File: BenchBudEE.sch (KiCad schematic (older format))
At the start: 0 parts

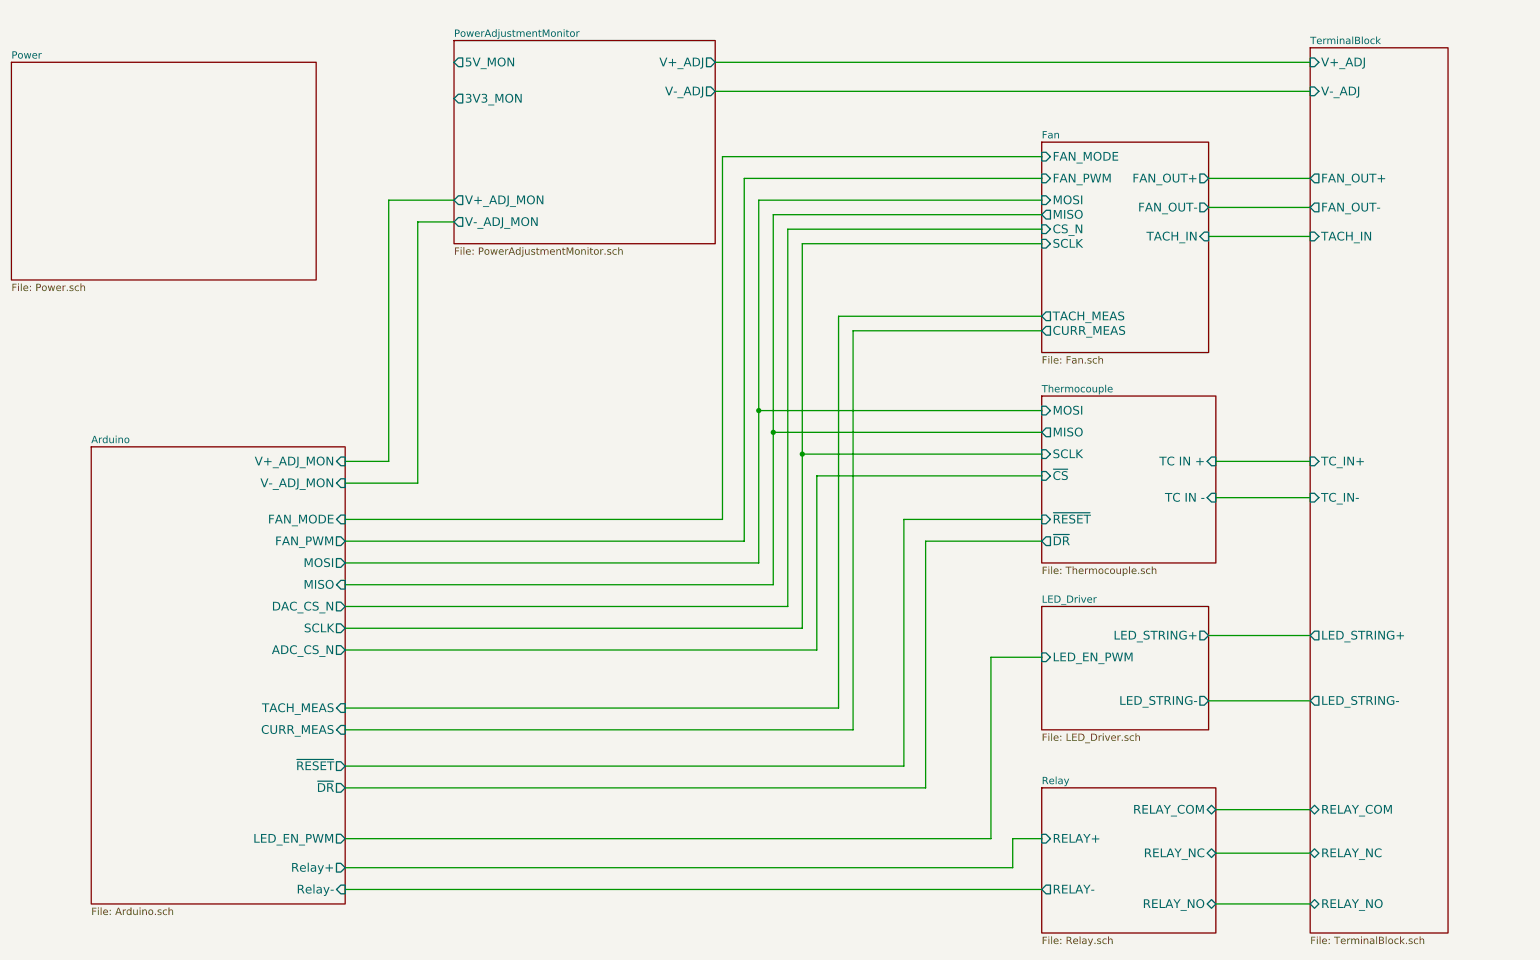
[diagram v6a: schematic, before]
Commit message: Fan driver: assc/placement
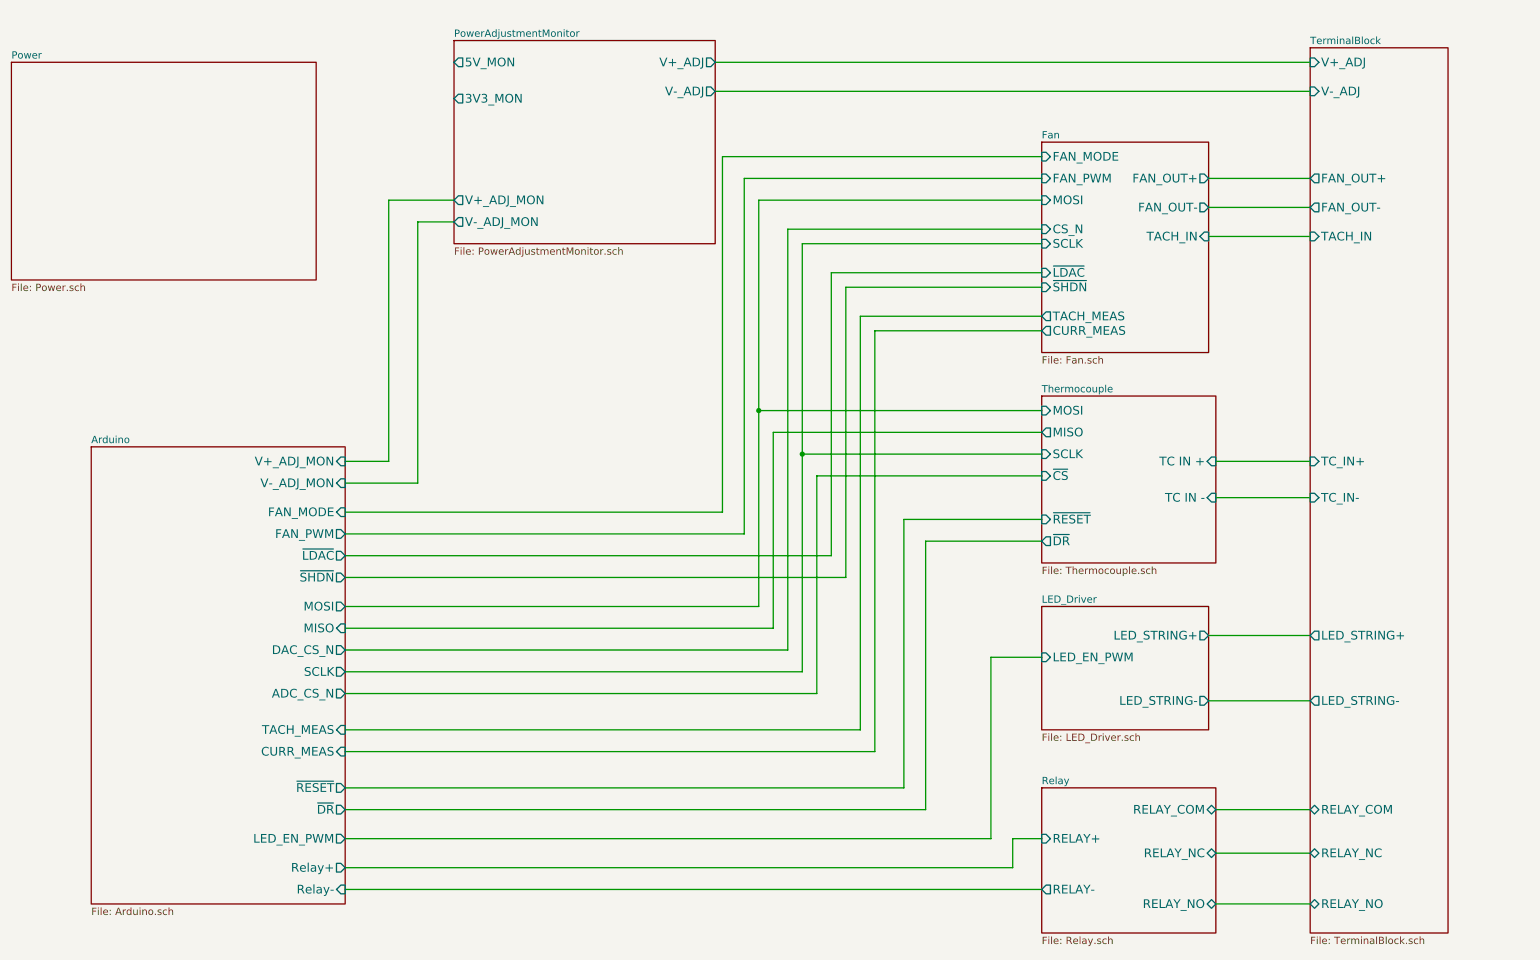
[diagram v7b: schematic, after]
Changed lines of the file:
@@
 Sheet 1 9
 Title ""
-Date "22 feb 2014"
+Date "23 feb 2014"
 Rev ""
 Comp ""
@@
 F1 "Fan.sch" 50
 F2 "MOSI" I L 8200 1950 60
-F3 "MISO" O L 8200 2050 60
-F4 "CS_N" I L 8200 2150 60
-F5 "SCLK" I L 8200 2250 60
-F6 "FAN_OUT+" O R 9350 1800 60
-F7 "TACH_IN" I R 9350 2200 60
-F8 "TACH_MEAS" O L 8200 2750 60
-F9 "CURR_MEAS" O L 8200 2850 60
-F10 "FAN_OUT-" O R 9350 2000 60
-F11 "FAN_PWM" I L 8200 1800 60
-F12 "FAN_MODE" I L 8200 1650 60
+F3 "CS_N" I L 8200 2150 60
+F4 "SCLK" I L 8200 2250 60
+F5 "FAN_OUT+" O R 9350 1800 60
+F6 "TACH_IN" I R 9350 2200 60
+F7 "TACH_MEAS" O L 8200 2750 60
+F8 "CURR_MEAS" O L 8200 2850 60
+F9 "FAN_OUT-" O R 9350 2000 60
+F10 "FAN_PWM" I L 8200 1800 60
+F11 "FAN_MODE" I L 8200 1650 60
+F12 "~LDAC" I L 8200 2450 60
+F13 "~SHDN" I L 8200 2550 60
 $EndSheet
 $Sheet
@@
 	3900 2100 4150 2100
 Wire Wire Line
-	3400 4300 6150 4300
-Wire Wire Line
-	6150 4300 6150 1800
+	3400 4250 6150 4250
+Wire Wire Line
+	6150 4250 6150 1800
 Wire Wire Line
 	6150 1800 8200 1800
 Wire Wire Line
-	6250 4450 3400 4450
-Wire Wire Line
-	6250 1950 6250 4450
+	6250 4750 3400 4750
+Wire Wire Line
+	6250 1950 6250 4750
 Wire Wire Line
 	6250 1950 8200 1950
 Wire Wire Line
-	6350 4600 3400 4600
-Wire Wire Line
-	6350 2050 6350 4600
-Wire Wire Line
-	6350 2050 8200 2050
-Wire Wire Line
-	3400 4750 6450 4750
-Wire Wire Line
-	6450 4750 6450 2150
+	3400 5050 6450 5050
+Wire Wire Line
+	6450 5050 6450 2150
 Wire Wire Line
 	6450 2150 8200 2150
 Wire Wire Line
-	6550 4900 3400 4900
-Wire Wire Line
-	6550 2250 6550 4900
+	6550 5200 3400 5200
+Wire Wire Line
+	6550 2250 6550 5200
 Wire Wire Line
 	6550 2250 8200 2250
@@
 Wire Wire Line
 	8200 3550 6350 3550
-Connection ~ 6350 3550
 Wire Wire Line
 	8200 3700 6550 3700
 Connection ~ 6550 3700
 Wire Wire Line
-	3400 5050 6650 5050
-Wire Wire Line
-	6650 5050 6650 3850
+	3400 5350 6650 5350
+Wire Wire Line
+	6650 5350 6650 3850
 Wire Wire Line
 	6650 3850 8200 3850
-$Sheet
-S 1650 3650 1750 3150
-U 52F2E3BD
-F0 "Arduino" 50
-F1 "Arduino.sch" 50
-F2 "Relay+" O R 3400 6550 60
-F3 "Relay-" I R 3400 6700 60
-F4 "V+_ADJ_MON" I R 3400 3750 60
-F5 "V-_ADJ_MON" I R 3400 3900 60
-F6 "MOSI" O R 3400 4450 60
-F7 "MISO" I R 3400 4600 60
-F8 "SCLK" O R 3400 4900 60
-F9 "TACH_MEAS" I R 3400 5450 60
-F10 "CURR_MEAS" I R 3400 5600 60
-F11 "LED_EN_PWM" O R 3400 6350 60
-F12 "DAC_CS_N" O R 3400 4750 60
-F13 "ADC_CS_N" O R 3400 5050 60
-F14 "FAN_PWM" O R 3400 4300 60
-F15 "FAN_MODE" I R 3400 4150 60
-F16 "~RESET" O R 3400 5850 60
-F17 "~DR" O R 3400 6000 60
-$EndSheet
-Wire Wire Line
-	3400 5450 6800 5450
-Wire Wire Line
-	6800 5450 6800 2750
-Wire Wire Line
-	6800 2750 8200 2750
-Wire Wire Line
-	8200 2850 6900 2850
-Wire Wire Line
-	6900 2850 6900 5600
-Wire Wire Line
-	6900 5600 3400 5600
+Wire Wire Line
+	3400 5600 6950 5600
+Wire Wire Line
+	6950 5600 6950 2750
+Wire Wire Line
+	6950 2750 8200 2750
+Wire Wire Line
+	8200 2850 7050 2850
+Wire Wire Line
+	7050 2850 7050 5750
+Wire Wire Line
+	7050 5750 3400 5750
 Wire Wire Line
 	3400 6350 7850 6350
@@
 	8200 1650 6000 1650
 Wire Wire Line
-	6000 1650 6000 4150
-Wire Wire Line
-	6000 4150 3400 4150
+	6000 1650 6000 4100
+Wire Wire Line
+	6000 4100 3400 4100
 $Sheet
 S 8200 6000 1200 1000
@@
 $EndSheet
 Wire Wire Line
-	3400 5850 7250 5850
-Wire Wire Line
-	7250 5850 7250 4150
+	3400 6000 7250 6000
+Wire Wire Line
+	7250 6000 7250 4150
 Wire Wire Line
 	7250 4150 8200 4150
 Wire Wire Line
-	3400 6000 7400 6000
-Wire Wire Line
-	7400 6000 7400 4300
+	3400 6150 7400 6150
+Wire Wire Line
+	7400 6150 7400 4300
 Wire Wire Line
 	7400 4300 8200 4300
+Wire Wire Line
+	6350 3550 6350 4900
+Wire Wire Line
+	6350 4900 3400 4900
+$Sheet
+S 1650 3650 1750 3150
+U 52F2E3BD
+F0 "Arduino" 50
+F1 "Arduino.sch" 50
+F2 "Relay+" O R 3400 6550 60
+F3 "Relay-" I R 3400 6700 60
+F4 "V+_ADJ_MON" I R 3400 3750 60
+F5 "V-_ADJ_MON" I R 3400 3900 60
+F6 "MOSI" O R 3400 4750 60
+F7 "MISO" I R 3400 4900 60
+F8 "SCLK" O R 3400 5200 60
+F9 "TACH_MEAS" I R 3400 5600 60
+F10 "CURR_MEAS" I R 3400 5750 60
+F11 "LED_EN_PWM" O R 3400 6350 60
+F12 "DAC_CS_N" O R 3400 5050 60
+F13 "ADC_CS_N" O R 3400 5350 60
+F14 "FAN_PWM" O R 3400 4250 60
+F15 "FAN_MODE" I R 3400 4100 60
+F16 "~RESET" O R 3400 6000 60
+F17 "~DR" O R 3400 6150 60
+F18 "~LDAC" O R 3400 4400 60
+F19 "~SHDN" O R 3400 4550 60
+$EndSheet
+Wire Wire Line
+	8200 2450 6750 2450
+Wire Wire Line
+	6750 2450 6750 4400
+Wire Wire Line
+	6750 4400 3400 4400
+Wire Wire Line
+	8200 2550 6850 2550
+Wire Wire Line
+	6850 2550 6850 4550
+Wire Wire Line
+	6850 4550 3400 4550
 $EndSCHEMATC
